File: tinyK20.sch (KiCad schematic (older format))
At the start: 78 parts, among them CON1 USB-MINI-B, P1 CONN_1, P10 CONN_1, P11 CONN_1, P12 CONN_1, P13 CONN_1, P14 CONN_1, P15 CONN_1, P16 CONN_1, P17 CONN_1, P18 CONN_1, P19 CONN_1, P2 CONN_1, P20 CONN_1, P21 CONN_1, P22 CONN_1, P23 CONN_1, P24 CONN_1, P25 CONN_1, P26 CONN_1, P27 CONN_1, P28 CONN_1, P29 CONN_1, P3 CONN_1, P30 CONN_1, P31 CONN_1, P32 CONN_1, P33 CONN_1, P34 CONN_1, P35 CONN_5X2, P36 CONN_1, P37 CONN_1, P38 CONN_5X2, P4 CONN_1, P41 CONN_1, P5 CONN_1, P6 CONN_1, P7 CONN_1, P8 CONN_1, P9 CONN_1, SW1 SW_PUSH, U1 MK20DX128VFT5, U2 LT1129CST-3.3, U3 74LS126, X3 MOLEX-MICRO-SD, Y1 Crystal, Y2 Crystal_Small

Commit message: Simplify the board
Remove all breakout pin headers
remove SD card connector
redo the PCB layout
change the debug connector to through hole 1.27mm
change the resistor footprints to handsoldering ones
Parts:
- removed C12: 2.2u, Capacitors_SMD:C_0805, symbol C-RESCUE-tinyK20
- removed GND1, P1, P10, P11, P12, P13, P14, P15, P16, P17, P18, P19, P2, P20, P21, P22, P23, P27, P28, P29, P3, P30, P31, P33, P4, P41, P5, P6, P7, P8, P9: CONN_1, Connect:PIN1, symbol CONN_1
- removed P24, P25, P26, P32, P34, P36, P37: CONN_1, Connect:PINC, symbol CONN_1
- removed X3: MOLEX-MICRO-SD, Connect:SD_Card_Receptacle, symbol MOLEX-MICRO-SD
- added C14, C15: 22nF, Capacitors_SMD:C_0805, symbol C
- added R7: 1M, Resistors_SMD:R_1206_HandSoldering, symbol R
- D2: footprint LEDs:LED_0603 -> Resistors_SMD:R_1206
- P38: footprint Pin_Headers:Pin_Header_Straight_2x05_Pitch1.27mm -> Connect:CONN-2x5-1.27-SMT
- R1, R4, R6: footprint Resistors_SMD:R_0805 -> Resistors_SMD:R_1206_HandSoldering
- R2, R3: footprint Resistors_SMD:R_0805 -> Resistors_SMD:R_0603_HandSoldering
- R5: footprint Resistors_SMD:R_0805 -> Resistors_SMD:R_1206
- U1: symbol MK20DX128VFT5 -> MK20DX128VFT5-RESCUE-tinyK20
- VBATT1: footprint Connect:PIN1 -> Wire_Pads:SolderWirePad_single_1mmDrill
- Y1: footprint Crystals:ABM3 -> Housings_DFN_QFN:ABM3
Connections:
- net labels removed: +3.3V, PTC0, PTC1
- wire segments 230 -> 180
- no-connect marks 6 -> 23
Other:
- note removed: "opt. micro-SD card interface"
- moved on the sheet: JP2, JP3

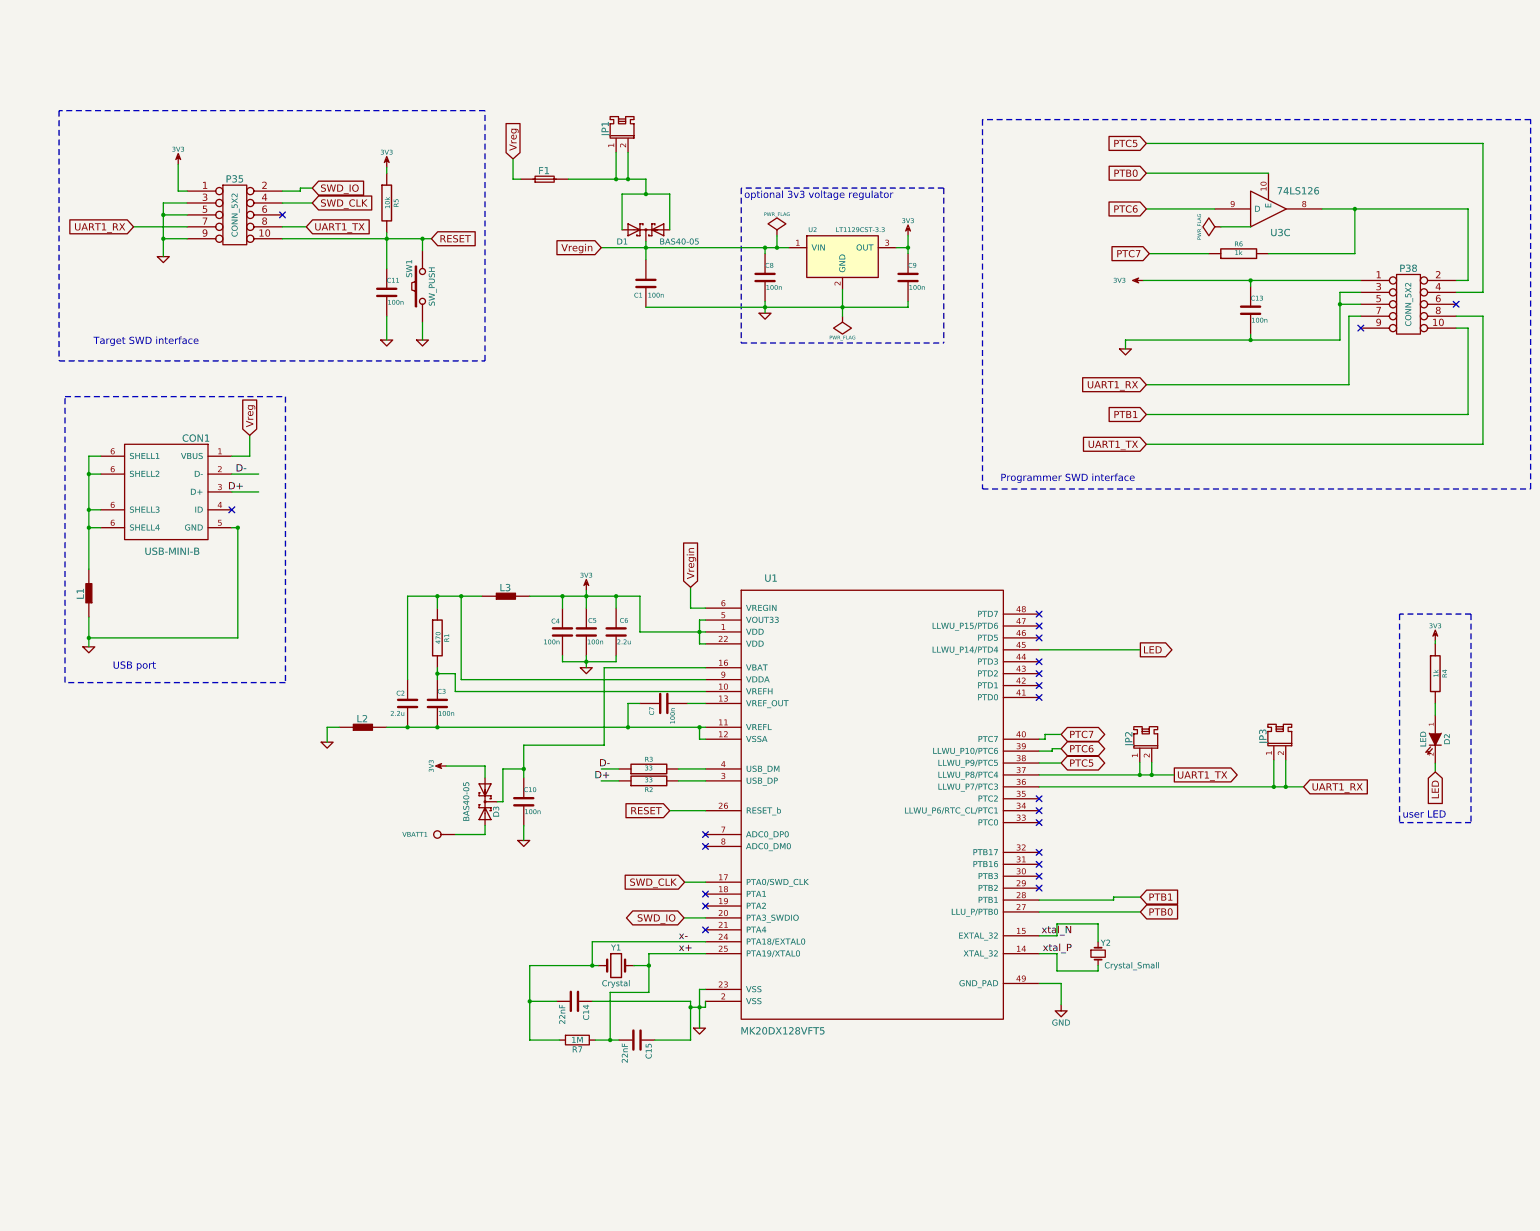
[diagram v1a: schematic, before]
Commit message: Add breakout headers and reroute the whole PCB board
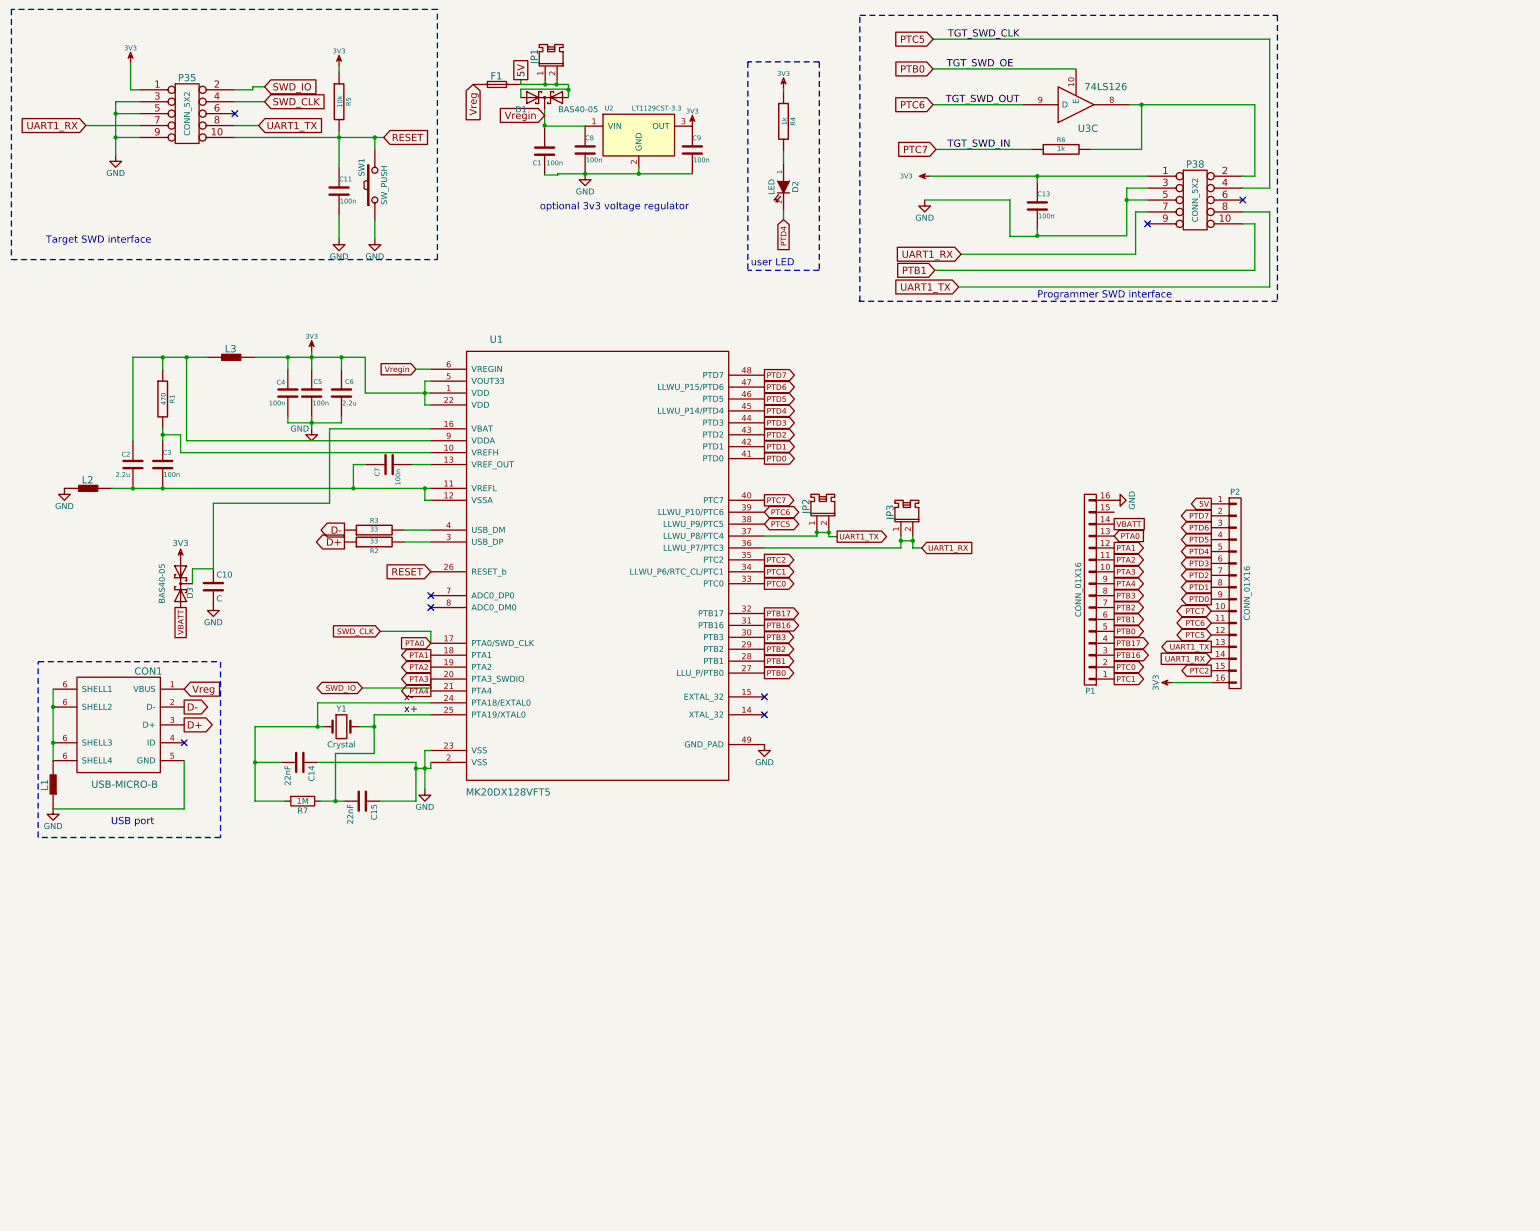
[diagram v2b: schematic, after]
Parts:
- removed C10: 100n, Capacitors_SMD:C_0805, symbol C-RESCUE-tinyK20
- removed VBATT1: CONN_1, Wire_Pads:SolderWirePad_single_1mmDrill, symbol CONN_1
- removed Y2: Crystal_Small, Crystals:Crystal_Round_Horizontal_3mm_BigPad, symbol Crystal_Small
- added C10: C, Capacitors_SMD:C_0805, symbol C
- added P1, P2: CONN_01X16, Pin_Headers:Pin_Header_Straight_1x16, symbol CONN_01X16
- CON1: value USB-MINI-B -> USB-MICRO-B
- F1: footprint Wire_Connections_Bridges:WireConnection_0.80mmDrill -> Resistors_SMD:R_0603
- L1, L2, L3: footprint Inductors_NEOSID:Neosid_Inductor_SM1206 -> Resistors_SMD:R_0603
- P38: footprint Connect:CONN-2x5-1.27-SMT -> Pin_Headers:CONN-2x5-1.27-SMT
- R1, R4, R6, R7: footprint Resistors_SMD:R_1206_HandSoldering -> Resistors_SMD:R_1206
- U1: footprint Housings_DFN_QFN:QFN-48-1EP_7x7mm_Pitch0.5mm -> Housings_QFP:TQFP-48-1EP_7x7mm_Pitch0.5mm
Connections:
- net 3V3: now also P2.16 (P16)
- net GND: now also C10.2, P1.16 (P16); no longer C13.2, CON1.5 (GND), P38.3, P38.5
- net PTB0: now also P1.5 (P5)
- net PTB1: now also P1.6 (P6)
- net PTC5: now also P2.12 (P12)
- net PTC6: now also P2.11 (P11)
- net PTC7: now also P2.10 (P10)
- net UART1_RX: now also P2.14 (P14)
- net UART1_TX: now also P2.13 (P13)
- net at D3.3 (K1K2), U1.16 (VBAT): now also C10.1
- net PTA1: now reaches U1.18 (PTA1)
- net PTA1: now also P1.12 (P12)
- net PTA2: now reaches U1.19 (PTA2)
- net PTA2: now also P1.11 (P11)
- net PTA4: now reaches U1.21 (PTA4)
- net PTA4: now also P1.9 (P9)
- net PTB2: now reaches U1.29 (PTB2)
- net PTB2: now also P1.7 (P7)
- net PTB3: now reaches U1.30 (PTB3)
- net PTB3: now also P1.8 (P8)
- net PTB16: now reaches U1.31 (PTB16)
- net PTB16: now also P1.3 (P3)
- net PTB17: now reaches U1.32 (PTB17)
- net PTB17: now also P1.4 (P4)
- net PTC0: now reaches U1.33 (PTC0)
- net PTC0: now also P1.2 (P2)
- net PTC1: now reaches U1.34 (LLWU_P6/RTC_CL/PTC1)
- net PTC1: now also P1.1 (P1)
- net PTC2: now reaches U1.35 (PTC2)
- net PTC2: now also P2.15 (P15)
- net PTD0: now reaches U1.41 (PTD0)
- net PTD0: now also P2.9 (P9)
- net PTD1: now reaches U1.42 (PTD1)
- net PTD1: now also P2.8 (P8)
- net PTD2: now reaches U1.43 (PTD2)
- net PTD2: now also P2.7 (P7)
- net PTD3: now reaches U1.44 (PTD3)
- net PTD3: now also P2.6 (P6)
- net PTD5: now reaches U1.46 (PTD5)
- net PTD5: now also P2.4 (P4)
- net PTD6: now reaches U1.47 (LLWU_P15/PTD6)
- net PTD6: now also P2.3 (P3)
- net PTD7: now reaches U1.48 (PTD7)
- net PTD7: now also P2.2 (P2)
- net 5V: now reaches D1.1 (A1), D1.2 (A2), F1.2, JP1.1, JP1.2
- net 5V: now also P2.1 (P1)
- net VBATT: now reaches D3.2 (A2)
- net VBATT: now also P1.14 (P14)
- net LED renamed PTD4
- net PTD4: now also P2.5 (P5)
- net SWD_CLK renamed PTA0
- net PTA0: now also P1.13 (P13)
- net SWD_IO renamed PTA3
- net PTA3: now also P1.10 (P10)
- net xtal_N: no longer names the net of U1.15 (EXTAL_32)
- net xtal_P: no longer names the net of U1.14 (XTAL_32)
- new net: C13.2, P38.3, P38.5
- no-connect marks 23 -> 8
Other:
- moved on the sheet: C1, C11, C13, C14, C15, C2, C3, C4, C5, C6, C7, C8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

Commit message: Make the board smaller
Switch the ABM2 crystal with a smaller Murata CSTE
Switch the debug line driver chip with a smaller footprint one
Adjust pin headers hopefully to breadboard friendly
Remove Jumpers on UART lines
Remove the 1Mohm resistor and two capacitors for the crystal. Not needed
Resize the entire board downwards and re-route the traces
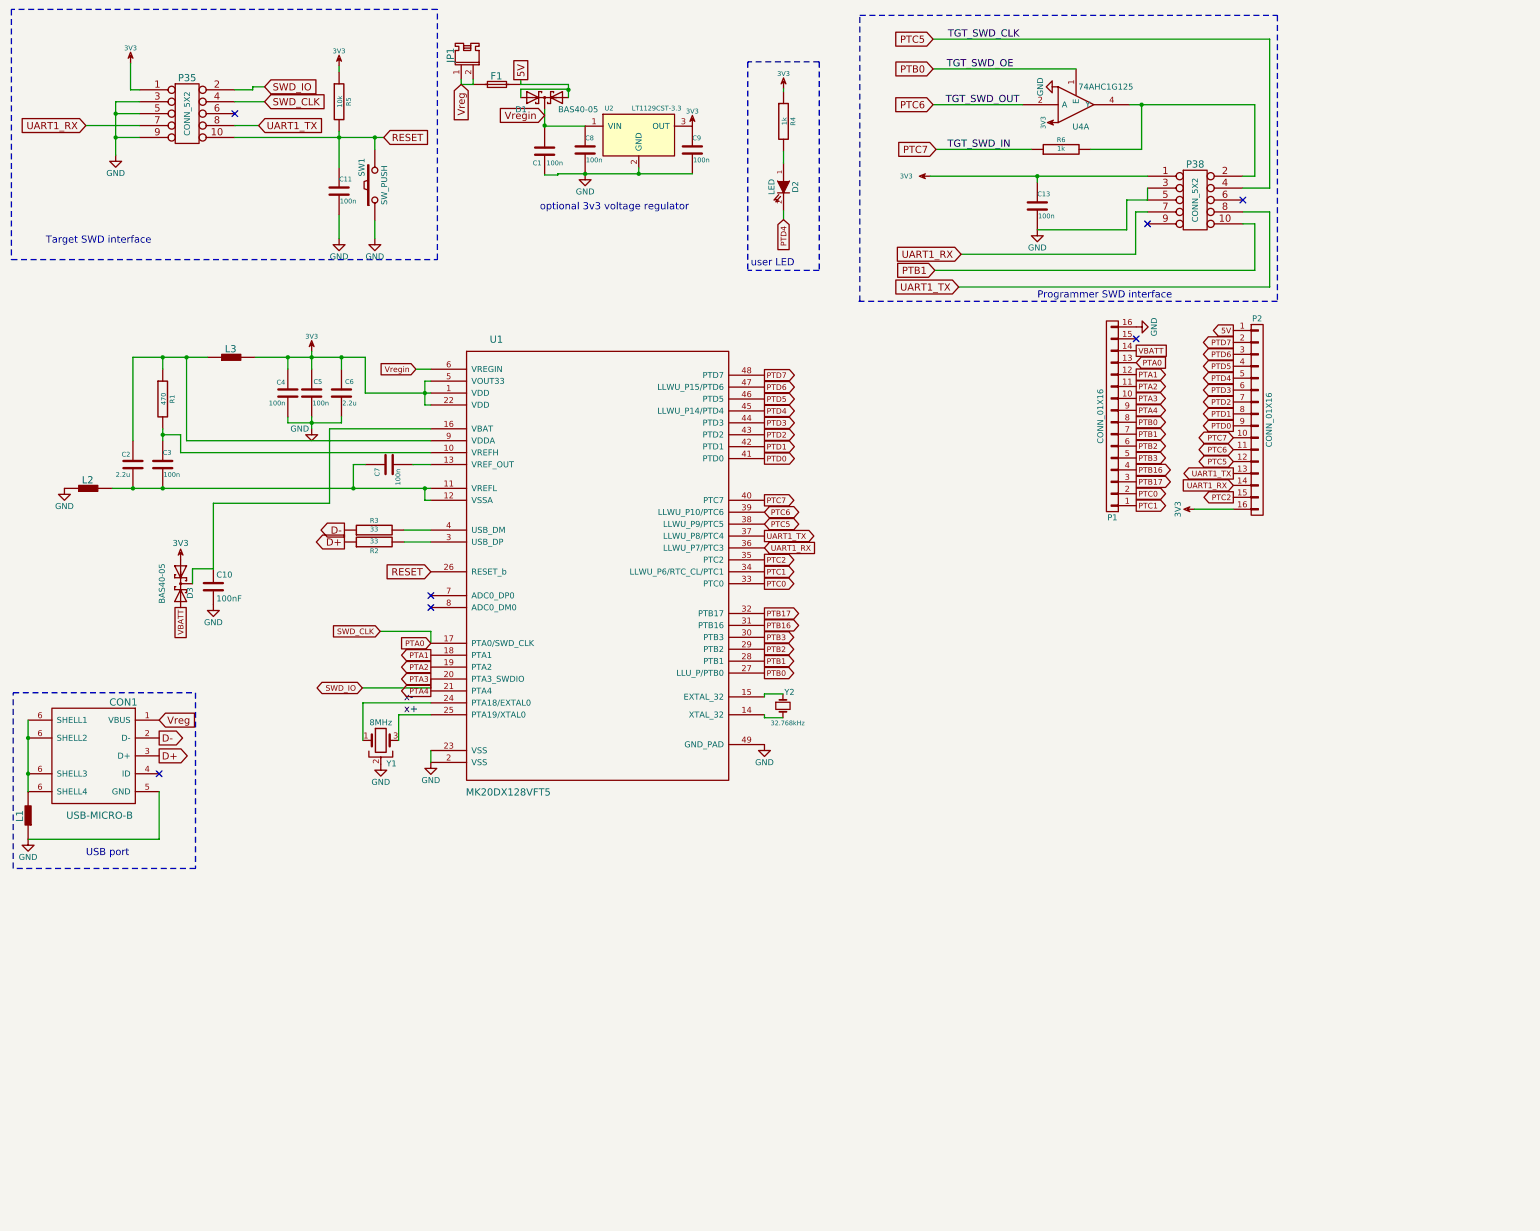
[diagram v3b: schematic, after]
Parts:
- removed C14, C15: 22nF, Capacitors_SMD:C_0805, symbol C
- removed JP2, JP3: JUMPER_F, Connect:PINHEAD1-2, symbol JUMPER_F
- removed R7: 1M, Resistors_SMD:R_1206, symbol R
- removed U3: 74LS126, SMD_Packages:SOIC-14_N, symbol 74LS126
- removed Y1: Crystal, Housings_DFN_QFN:ABM3, symbol Crystal
- added U4: 74AHC1G125, TO_SOT_Packages_SMD:SOT-353, symbol 74AHC1G125
- added Y1: 8MHz, Crystals:CERALOCK-CSTCE8M00G15L99-R0, symbol Crystal_GND2
- added Y2: 32.768kHz, Crystals:Crystal_Round_Horizontal_2mm, symbol Crystal_Small
- C10: value C -> 100nF
- JP1: footprint Connect:PINHEAD1-2 -> Pin_Headers:Pin_Header_Straight_1x02
- R1, R5: footprint Resistors_SMD:R_1206 -> Resistors_SMD:R_0805
- R2, R3: footprint Resistors_SMD:R_0603_HandSoldering -> Resistors_SMD:R_0603
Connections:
- net 3V3: now also U4.5 (VCC)
- net 5V: no longer JP1.1, JP1.2
- net GND: now also C13.2, CON1.5 (GND), P38.3, P38.5, U4.3 (GND), Y1.2
- net PTB0: now also P1.8 (P8), U4.1 (E); no longer P1.5 (P5)
- net PTB1: now also P1.7 (P7); no longer P1.6 (P6)
- net PTB16: now also P1.4 (P4); no longer P1.3 (P3)
- net PTB17: now also P1.3 (P3); no longer P1.4 (P4)
- net PTB2: now also P1.6 (P6); no longer P1.7 (P7)
- net PTB3: now also P1.5 (P5); no longer P1.8 (P8)
- net PTC6: now also U4.2 (A)
- net Vreg: now also JP1.1, JP1.2
- net x+: now also Y1.3
- net x-: now also Y1.1
- net at U1.14 (XTAL_32): now also Y2.2
- net at U1.15 (EXTAL_32): now also Y2.1
- net at P38.2, R6.2: now also U4.4 (Y)
- no-connect marks 8 -> 7
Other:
- moved on the sheet: CON1, L1, P1, P2
